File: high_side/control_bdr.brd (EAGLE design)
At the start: 100 x 80 mm, 46 parts

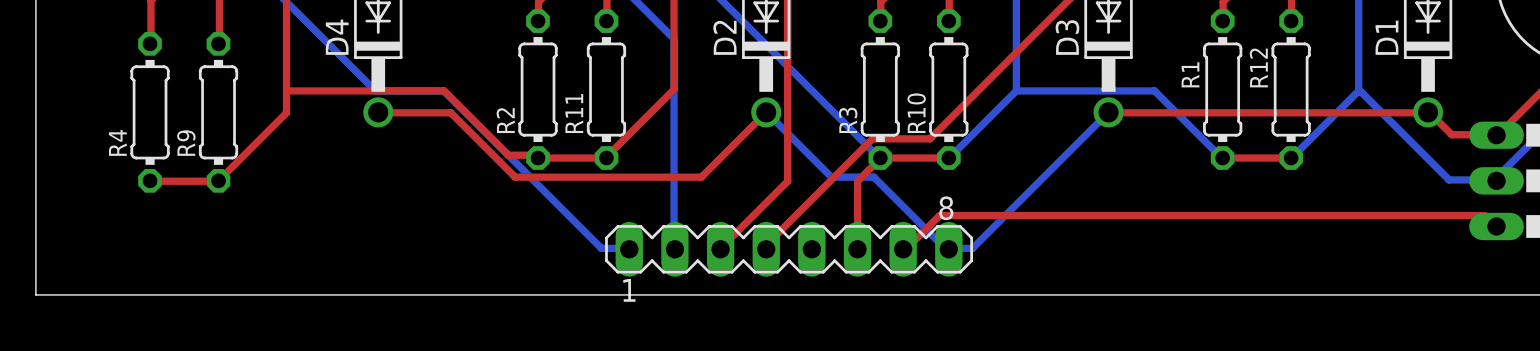
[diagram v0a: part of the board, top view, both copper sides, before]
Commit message: Rework dirs
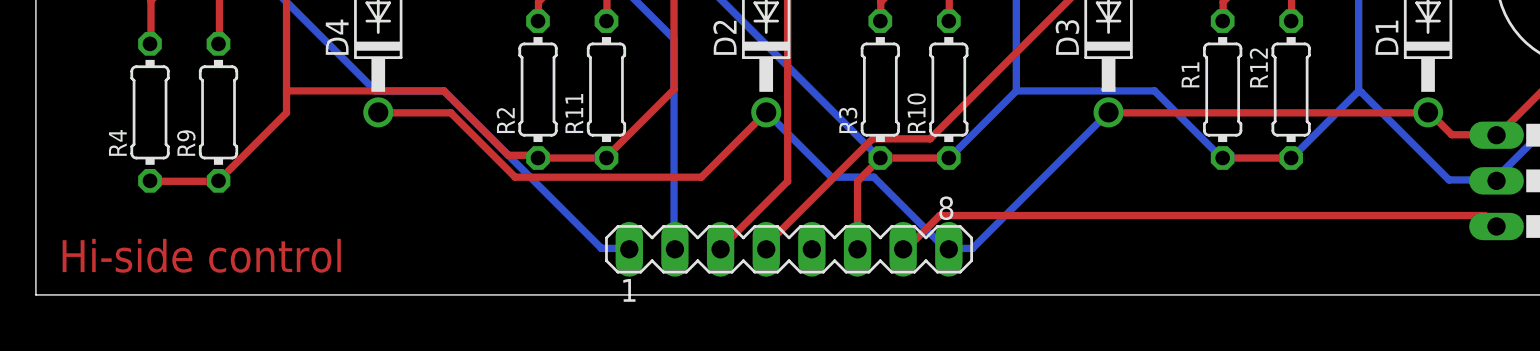
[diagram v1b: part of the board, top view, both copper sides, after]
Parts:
- R1, R2, R3, R4: value 330 -> 80
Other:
- board text added: "Hi-side control"
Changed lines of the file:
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@@
 <setting verticaltext="up"/>
 </settings>
-<grid distance="50" unitdist="mil" unit="mil" style="lines" multiple="1" display="no" altdistance="5" altunitdist="mil" altunit="mil"/>
+<grid distance="10" unitdist="mil" unit="mil" style="lines" multiple="1" display="no" altdistance="5" altunitdist="mil" altunit="mil"/>
 <layers>
 <layer number="1" name="Top" color="4" fill="1" visible="yes" active="yes"/>
@@
 <layer number="28" name="bValues" color="7" fill="1" visible="yes" active="yes"/>
 <layer number="29" name="tStop" color="7" fill="3" visible="yes" active="yes"/>
-<layer number="30" name="bStop" color="7" fill="6" visible="no" active="yes"/>
+<layer number="30" name="bStop" color="7" fill="6" visible="yes" active="yes"/>
 <layer number="31" name="tCream" color="7" fill="4" visible="no" active="yes"/>
 <layer number="32" name="bCream" color="7" fill="5" visible="no" active="yes"/>
-<layer number="33" name="tFinish" color="6" fill="3" visible="no" active="yes"/>
-<layer number="34" name="bFinish" color="6" fill="6" visible="no" active="yes"/>
+<layer number="33" name="tFinish" color="6" fill="3" visible="yes" active="yes"/>
+<layer number="34" name="bFinish" color="6" fill="6" visible="yes" active="yes"/>
 <layer number="35" name="tGlue" color="7" fill="4" visible="no" active="yes"/>
 <layer number="36" name="bGlue" color="7" fill="5" visible="no" active="yes"/>
@@
 <wire x1="85.09" y1="44.45" x2="97.79" y2="44.45" width="0.508" layer="46"/>
 <rectangle x1="88.9" y1="1.27" x2="99.06" y2="13.97" layer="1"/>
+<text x="1.27" y="1.27" size="1.778" layer="1">Hi-side control</text>
+<rectangle x1="88.9" y1="1.27" x2="99.06" y2="13.97" layer="29"/>
+<polygon width="0.4064" layer="29">
+<vertex x="97.79" y="78.74"/>
+<vertex x="97.79" y="64.77"/>
+<vertex x="96.52" y="63.5"/>
+<vertex x="74.93" y="63.5"/>
+<vertex x="73.66" y="64.77"/>
+<vertex x="68.58" y="64.77"/>
+<vertex x="66.04" y="67.31"/>
+<vertex x="66.04" y="78.74"/>
+</polygon>
+<polygon width="0.127" layer="29" spacing="0.254">
+<vertex x="56.134" y="56.896"/>
+<vertex x="56.134" y="61.976"/>
+<vertex x="47.752" y="70.358"/>
+<vertex x="45.212" y="72.898"/>
+<vertex x="45.212" y="74.168"/>
+<vertex x="43.688" y="75.692"/>
+<vertex x="42.418" y="75.692"/>
+<vertex x="41.402" y="74.676"/>
+<vertex x="41.402" y="74.422"/>
+<vertex x="41.402" y="71.12"/>
+<vertex x="52.324" y="60.198"/>
+<vertex x="52.324" y="56.896"/>
+<vertex x="53.34" y="55.88"/>
+<vertex x="53.594" y="55.626"/>
+<vertex x="54.864" y="55.626"/>
+</polygon>
+<polygon width="0.127" layer="29" spacing="0.254">
+<vertex x="37.338" y="73.152"/>
+<vertex x="37.338" y="74.168"/>
+<vertex x="36.068" y="75.438"/>
+<vertex x="34.29" y="75.438"/>
+<vertex x="33.274" y="74.422"/>
+<vertex x="33.274" y="74.168"/>
+<vertex x="33.274" y="71.628"/>
+<vertex x="35.814" y="69.088"/>
+<vertex x="35.814" y="57.15"/>
+<vertex x="37.084" y="55.88"/>
+<vertex x="38.608" y="55.88"/>
+<vertex x="39.624" y="56.896"/>
+<vertex x="39.624" y="70.612"/>
+<vertex x="37.338" y="72.898"/>
+</polygon>
+<polygon width="0.127" layer="29" spacing="0.254">
+<vertex x="18.542" y="60.452"/>
+<vertex x="18.542" y="56.642"/>
+<vertex x="17.272" y="55.372"/>
+<vertex x="14.986" y="55.372"/>
+<vertex x="13.716" y="56.642"/>
+<vertex x="13.716" y="58.928"/>
+<vertex x="3.81" y="68.834"/>
+<vertex x="3.81" y="75.692"/>
+<vertex x="3.81" y="75.946"/>
+<vertex x="5.334" y="77.47"/>
+<vertex x="5.588" y="77.724"/>
+<vertex x="7.112" y="77.724"/>
+<vertex x="8.89" y="75.946"/>
+<vertex x="8.89" y="70.866"/>
+<vertex x="18.542" y="61.214"/>
+<vertex x="18.542" y="60.706"/>
+</polygon>
+<polygon width="0.127" layer="30" spacing="0.254">
+<vertex x="81.788" y="53.848"/>
+<vertex x="81.788" y="49.53"/>
+<vertex x="81.28" y="49.022"/>
+<vertex x="68.072" y="49.022"/>
+<vertex x="67.818" y="48.768"/>
+<vertex x="67.818" y="40.132"/>
+<vertex x="61.722" y="40.132"/>
+<vertex x="61.722" y="49.022"/>
+<vertex x="51.308" y="49.022"/>
+<vertex x="51.308" y="40.132"/>
+<vertex x="45.212" y="40.132"/>
+<vertex x="45.212" y="49.022"/>
+<vertex x="34.798" y="49.022"/>
+<vertex x="34.798" y="40.386"/>
+<vertex x="34.544" y="40.132"/>
+<vertex x="28.956" y="40.132"/>
+<vertex x="28.702" y="40.386"/>
+<vertex x="28.702" y="49.022"/>
+<vertex x="13.208" y="49.022"/>
+<vertex x="13.208" y="40.64"/>
+<vertex x="12.7" y="40.132"/>
+<vertex x="7.366" y="40.132"/>
+<vertex x="7.112" y="40.386"/>
+<vertex x="7.112" y="65.024"/>
+<vertex x="7.366" y="65.278"/>
+<vertex x="17.272" y="65.278"/>
+<vertex x="17.272" y="78.486"/>
+<vertex x="17.526" y="78.74"/>
+<vertex x="23.622" y="78.74"/>
+<vertex x="24.638" y="77.724"/>
+<vertex x="24.638" y="61.976"/>
+<vertex x="23.114" y="60.452"/>
+<vertex x="13.97" y="60.452"/>
+<vertex x="13.208" y="59.69"/>
+<vertex x="13.208" y="55.88"/>
+<vertex x="15.24" y="53.848"/>
+<vertex x="15.494" y="53.848"/>
+</polygon>
+<polygon width="0.127" layer="29" spacing="0.254">
+<vertex x="72.644" y="58.166"/>
+<vertex x="72.644" y="56.896"/>
+<vertex x="71.374" y="55.626"/>
+<vertex x="66.294" y="55.626"/>
+<vertex x="49.276" y="72.644"/>
+<vertex x="49.276" y="74.422"/>
+<vertex x="50.546" y="75.692"/>
+<vertex x="51.562" y="75.692"/>
+<vertex x="51.816" y="75.438"/>
+<vertex x="67.818" y="59.436"/>
+<vertex x="68.072" y="59.436"/>
+<vertex x="71.374" y="59.436"/>
+</polygon>
 </plain>
 <attributes>
@@
 <attribute name="POPULARITY" value="0" x="-13.97" y="-49.53" size="1.778" layer="27" rot="R270" display="off"/>
 </element>
-<element name="R1" library="rcl" library_urn="urn:adsk.eagle:library:334" package="0204/7" package3d_urn="urn:adsk.eagle:package:23498/2" value="330" x="66.04" y="11.43" smashed="yes" rot="R90">
+<element name="R1" library="rcl" library_urn="urn:adsk.eagle:library:334" package="0204/7" package3d_urn="urn:adsk.eagle:package:23498/2" value="80" x="66.04" y="11.43" smashed="yes" rot="R90">
 <attribute name="NAME" x="64.7446" y="11.43" size="0.9906" layer="25" ratio="10" rot="R90"/>
 <attribute name="POPULARITY" value="79" x="134.62" y="41.91" size="1.778" layer="27" rot="R90" display="off"/>
@@
 <attribute name="VALUE" x="70.3326" y="9.8044" size="0.9906" layer="27" ratio="10" rot="R90"/>
 </element>
-<element name="R2" library="rcl" library_urn="urn:adsk.eagle:library:334" package="0204/7" package3d_urn="urn:adsk.eagle:package:23498/2" value="330" x="27.94" y="11.43" smashed="yes" rot="R90">
+<element name="R2" library="rcl" library_urn="urn:adsk.eagle:library:334" package="0204/7" package3d_urn="urn:adsk.eagle:package:23498/2" value="80" x="27.94" y="11.43" smashed="yes" rot="R90">
 <attribute name="NAME" x="26.6446" y="8.89" size="0.9906" layer="25" ratio="10" rot="R90"/>
 <attribute name="POPULARITY" value="79" x="96.52" y="52.07" size="1.778" layer="27" rot="R90" display="off"/>
@@
 <attribute name="VALUE" x="28.4226" y="9.8044" size="0.9906" layer="27" ratio="10" rot="R90"/>
 </element>
-<element name="R3" library="rcl" library_urn="urn:adsk.eagle:library:334" package="0204/7" package3d_urn="urn:adsk.eagle:package:23498/2" value="330" x="46.99" y="11.43" smashed="yes" rot="R90">
+<element name="R3" library="rcl" library_urn="urn:adsk.eagle:library:334" package="0204/7" package3d_urn="urn:adsk.eagle:package:23498/2" value="80" x="46.99" y="11.43" smashed="yes" rot="R90">
 <attribute name="NAME" x="45.6946" y="8.89" size="0.9906" layer="25" ratio="10" rot="R90"/>
 <attribute name="POPULARITY" value="79" x="115.57" y="62.23" size="1.778" layer="27" rot="R90" display="off"/>
@@
 <attribute name="VALUE" x="47.4726" y="9.8044" size="0.9906" layer="27" ratio="10" rot="R90"/>
 </element>
-<element name="R4" library="rcl" library_urn="urn:adsk.eagle:library:334" package="0204/7" package3d_urn="urn:adsk.eagle:package:23498/2" value="330" x="6.35" y="10.16" smashed="yes" rot="R90">
+<element name="R4" library="rcl" library_urn="urn:adsk.eagle:library:334" package="0204/7" package3d_urn="urn:adsk.eagle:package:23498/2" value="80" x="6.35" y="10.16" smashed="yes" rot="R90">
 <attribute name="NAME" x="5.0546" y="7.62" size="0.9906" layer="25" ratio="10" rot="R90"/>
 <attribute name="POPULARITY" value="79" x="74.93" y="71.12" size="1.778" layer="27" rot="R90" display="off"/>
@@
 <wire x1="16.6878" y1="36.8808" x2="16.51" y2="36.83" width="0.4064" layer="1"/>
 <wire x1="34.29" y1="36.8808" x2="34.29" y2="36.83" width="0.4064" layer="1"/>
-<wire x1="77.4954" y1="10.2108" x2="77.47" y2="10.16" width="0.4064" layer="1"/>
 <wire x1="53.34" y1="44.4246" x2="53.34" y2="36.83" width="0.4064" layer="1"/>
 <wire x1="54.2544" y1="45.339" x2="53.34" y2="44.4246" width="0.4064" layer="1"/>
